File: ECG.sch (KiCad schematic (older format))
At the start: 8 parts

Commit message: Completed power circuits
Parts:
- gave numbers to parts that had none: 3
- renumbered 9V to 9V1, GND to GND1
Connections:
- net +9V: now reaches 9V1.1, C1.1, U2.1 (IN)
- net 2.5V: no longer names the net of C4.1, U1.6 (OUT)
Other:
- note added: "Voltage Reference"
- moved on the sheet: 9V1, C1, C2, C3, C4, GND1, U1, U2
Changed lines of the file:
@@
 encoding utf-8
 Sheet 1 1
-Title ""
+Title "Power"
 Date ""
 Rev ""
@@
 $EndDescr
 $Comp
-L Regulator_Linear:L7805 U?
+L Device:CP1 C2
+U 1 1 5F980DB6
+P 5825 2775
+F 0 "C2" H 5925 2875 50  0000 L CNN
+F 1 "10uF" H 5900 2700 50  0000 L CNN
+F 2 "" H 5825 2775 50  0001 C CNN
+F 3 "~" H 5825 2775 50  0001 C CNN
+	1    5825 2775
+	1    0    0    -1
+$EndComp
+$Comp
+L Device:CP1 C3
+U 1 1 5F9833A5
+P 6200 2775
+F 0 "C3" H 6315 2821 50  0000 L CNN
+F 1 "100nF" H 6315 2730 50  0000 L CNN
+F 2 "" H 6200 2775 50  0001 C CNN
+F 3 "~" H 6200 2775 50  0001 C CNN
+	1    6200 2775
+	1    0    0    -1
+$EndComp
+$Comp
+L Mechanical:MountingHole_Pad 9V1
+U 1 1 5F985E28
+P 4375 2625
+F 0 "9V1" V 4381 2777 50  0000 L CNN
+F 1 "MountingHole_Pad" V 4475 2583 50  0001 L CNN
+F 2 "" H 4375 2625 50  0001 C CNN
+F 3 "~" H 4375 2625 50  0001 C CNN
+	1    4375 2625
+	0    -1   -1   0
+$EndComp
+$Comp
+L Mechanical:MountingHole_Pad GND1
+U 1 1 5F98A564
+P 4375 2925
+F 0 "GND1" V 4475 2974 50  0000 L CNN
+F 1 "MountingHole_Pad" V 4475 2883 50  0001 L CNN
+F 2 "" H 4375 2925 50  0001 C CNN
+F 3 "~" H 4375 2925 50  0001 C CNN
+	1    4375 2925
+	0    -1   -1   0
+$EndComp
+Text Notes 4936 3380 0    118  ~ 0
+Input Power
+Text Notes 4808 5084 0    50   ~ 0
+Voltage Reference
+Wire Notes Line
+	3960 2350 3960 5784
+Wire Notes Line
+	3960 5784 6958 5784
+Wire Notes Line
+	6958 5784 6958 2118
+Wire Notes Line
+	6958 2118 3960 2118
+Wire Notes Line
+	3960 2118 3960 2348
+$Comp
+L power:GND #PWR0102
+U 1 1 5F9A88EF
+P 5400 2925
+F 0 "#PWR0102" H 5400 2675 50  0001 C CNN
+F 1 "GND" H 5405 2752 50  0000 C CNN
+F 2 "" H 5400 2925 50  0001 C CNN
+F 3 "" H 5400 2925 50  0001 C CNN
+	1    5400 2925
+	1    0    0    -1
+$EndComp
+$Comp
+L power:+9V #PWR0101
+U 1 1 5F9AB243
+P 4475 2625
+F 0 "#PWR0101" H 4475 2475 50  0001 C CNN
+F 1 "+9V" H 4490 2798 50  0000 C CNN
+F 2 "" H 4475 2625 50  0001 C CNN
+F 3 "" H 4475 2625 50  0001 C CNN
+	1    4475 2625
+	1    0    0    -1
+$EndComp
+$Comp
+L power:PWR_FLAG #FLG01
+U 1 1 5F9B3B5D
+P 4875 2625
+F 0 "#FLG01" H 4875 2700 50  0001 C CNN
+F 1 "PWR_FLAG" H 4875 2798 50  0000 C CNN
+F 2 "" H 4875 2625 50  0001 C CNN
+F 3 "~" H 4875 2625 50  0001 C CNN
+	1    4875 2625
+	1    0    0    -1
+$EndComp
+$Comp
+L Device:CP1 C4
+U 1 1 5F991542
+P 5475 4475
+F 0 "C4" H 5590 4521 50  0000 L CNN
+F 1 "1uF" H 5590 4430 50  0000 L CNN
+F 2 "" H 5475 4475 50  0001 C CNN
+F 3 "~" H 5475 4475 50  0001 C CNN
+	1    5475 4475
+	1    0    0    -1
+$EndComp
+Wire Wire Line
+	4825 4625 4750 4625
+Text GLabel 4750 4625 0    50   Input ~ 0
+5V
+$Comp
+L Reference_Voltage:ADR4525 U1
+U 1 1 5F98E0E5
+P 5125 4525
+F 0 "U1" V 4836 4525 50  0000 C CNN
+F 1 "ADR4525" V 4745 4525 50  0000 C CNN
+F 2 "Package_SO:SOIC-8_3.9x4.9mm_P1.27mm" H 5225 4225 50  0001 C CIN
+F 3 "https://www.analog.com/media/en/technical-documentation/data-sheets/ADR4520_4525_4530_4533_4540_4550.pdf" H 5225 4175 50  0001 C CIN
+	1    5125 4525
+	0    -1   -1   0
+$EndComp
+Wire Wire Line
+	5125 4225 5475 4225
+Wire Wire Line
+	5475 4225 5475 4325
+$Comp
+L power:GND #PWR02
+U 1 1 5F9D2687
+P 5475 4625
+F 0 "#PWR02" H 5475 4375 50  0001 C CNN
+F 1 "GND" H 5480 4452 50  0000 C CNN
+F 2 "" H 5475 4625 50  0001 C CNN
+F 3 "" H 5475 4625 50  0001 C CNN
+	1    5475 4625
+	1    0    0    -1
+$EndComp
+$Comp
+L Regulator_Linear:L7805 U2
 U 1 1 5F977B65
-P 2050 1200
-F 0 "U?" H 2050 1442 50  0000 C CNN
-F 1 "L7805" H 2050 1351 50  0000 C CNN
-F 2 "" H 2075 1050 50  0001 L CIN
-F 3 "http://www.st.com/content/ccc/resource/technical/document/datasheet/41/4f/b3/b0/12/d4/47/88/CD00000444.pdf/files/CD00000444.pdf/jcr:content/translations/en.CD00000444.pdf" H 2050 1150 50  0001 C CNN
-	1    2050 1200
+P 5400 2625
+F 0 "U2" H 5400 2867 50  0000 C CNN
+F 1 "L7805" H 5400 2776 50  0000 C CNN
+F 2 "" H 5425 2475 50  0001 L CIN
+F 3 "http://www.st.com/content/ccc/resource/technical/document/datasheet/41/4f/b3/b0/12/d4/47/88/CD00000444.pdf/files/CD00000444.pdf/jcr:content/translations/en.CD00000444.pdf" H 5400 2575 50  0001 C CNN
+	1    5400 2625
 	1    0    0    -1
 $EndComp
@@
 L Device:CP1 C1
 U 1 1 5F97B8CA
-P 1550 1350
-F 0 "C1" H 1665 1396 50  0000 L CNN
-F 1 "100uF" H 1665 1305 50  0000 L CNN
-F 2 "" H 1550 1350 50  0001 C CNN
-F 3 "~" H 1550 1350 50  0001 C CNN
-	1    1550 1350
-	1    0    0    -1
-$EndComp
-$Comp
-L Device:CP1 C2
-U 1 1 5F980DB6
-P 2550 1350
-F 0 "C2" H 2665 1396 50  0000 L CNN
-F 1 "10uF" H 2665 1305 50  0000 L CNN
-F 2 "" H 2550 1350 50  0001 C CNN
-F 3 "~" H 2550 1350 50  0001 C CNN
-	1    2550 1350
-	1    0    0    -1
-$EndComp
-$Comp
-L Device:CP1 C3
-U 1 1 5F9833A5
-P 2900 1350
-F 0 "C3" H 3015 1396 50  0000 L CNN
-F 1 "100nF" H 3015 1305 50  0000 L CNN
-F 2 "" H 2900 1350 50  0001 C CNN
-F 3 "~" H 2900 1350 50  0001 C CNN
-	1    2900 1350
-	1    0    0    -1
-$EndComp
-$Comp
-L power:GND #PWR?
-U 1 1 5F983C07
-P 2050 1500
-F 0 "#PWR?" H 2050 1250 50  0001 C CNN
-F 1 "GND" H 2055 1327 50  0000 C CNN
-F 2 "" H 2050 1500 50  0001 C CNN
-F 3 "" H 2050 1500 50  0001 C CNN
-	1    2050 1500
-	1    0    0    -1
-$EndComp
-Wire Wire Line
-	1550 1500 2050 1500
-Connection ~ 2050 1500
-Wire Wire Line
-	2900 1500 2550 1500
-Wire Wire Line
-	2050 1500 2550 1500
-Connection ~ 2550 1500
-Wire Wire Line
-	1550 1200 1750 1200
-Wire Wire Line
-	2350 1200 2550 1200
-Wire Wire Line
-	2900 1200 2550 1200
-Connection ~ 2550 1200
-$Comp
-L Mechanical:MountingHole_Pad 9V
-U 1 1 5F985E28
-P 1050 1200
-F 0 "9V" V 1150 1249 50  0000 L CNN
-F 1 "MountingHole_Pad" V 1150 1158 50  0001 L CNN
-F 2 "" H 1050 1200 50  0001 C CNN
-F 3 "~" H 1050 1200 50  0001 C CNN
-	1    1050 1200
-	0    -1   -1   0
-$EndComp
-$Comp
-L Mechanical:MountingHole_Pad GND
-U 1 1 5F98A564
-P 1050 1500
-F 0 "GND" V 1150 1549 50  0000 L CNN
-F 1 "MountingHole_Pad" V 1150 1458 50  0001 L CNN
-F 2 "" H 1050 1500 50  0001 C CNN
-F 3 "~" H 1050 1500 50  0001 C CNN
-	1    1050 1500
-	0    -1   -1   0
-$EndComp
-Wire Wire Line
-	1150 1200 1550 1200
-Connection ~ 1550 1200
-Wire Wire Line
-	1550 1500 1150 1500
-Connection ~ 1550 1500
-Text Label 2900 1200 0    50   ~ 0
+P 4875 2775
+F 0 "C1" H 4990 2821 50  0000 L CNN
+F 1 "100uF" H 4950 2700 50  0000 L CNN
+F 2 "" H 4875 2775 50  0001 C CNN
+F 3 "~" H 4875 2775 50  0001 C CNN
+	1    4875 2775
+	1    0    0    -1
+$EndComp
+Wire Wire Line
+	4475 2925 4875 2925
+Connection ~ 4875 2925
+Wire Wire Line
+	5400 2925 4875 2925
+Connection ~ 5400 2925
+Wire Wire Line
+	4875 2625 4475 2625
+Connection ~ 4875 2625
+Connection ~ 4475 2625
+Wire Wire Line
+	4875 2625 5100 2625
+Wire Wire Line
+	5700 2625 5825 2625
+Wire Wire Line
+	5400 2925 5825 2925
+Wire Wire Line
+	6200 2925 5825 2925
+Connection ~ 5825 2925
+Wire Wire Line
+	6200 2625 5825 2625
+Connection ~ 5825 2625
+Text GLabel 6200 2625 2    50   Input Italic 0
 5V
-Text Notes 1600 1950 0    118  ~ 0
-Input Power
-$Comp
-L Reference_Voltage:ADR4525 U?
-U 1 1 5F98E0E5
-P 1800 3100
-F 0 "U?" V 1511 3100 50  0000 C CNN
-F 1 "ADR4525" V 1420 3100 50  0000 C CNN
-F 2 "Package_SO:SOIC-8_3.9x4.9mm_P1.27mm" H 1900 2800 50  0001 C CIN
-F 3 "https://www.analog.com/media/en/technical-documentation/data-sheets/ADR4520_4525_4530_4533_4540_4550.pdf" H 1900 2750 50  0001 C CIN
-	1    1800 3100
-	0    -1   -1   0
-$EndComp
-Text Label 1400 3200 0    50   ~ 0
-5V
-Wire Wire Line
-	1400 3200 1500 3200
-Text Label 2200 3200 0    50   ~ 0
-GND
-Wire Wire Line
-	2100 3200 2200 3200
-$Comp
-L Device:CP1 C?
-U 1 1 5F991542
-P 2200 3000
-F 0 "C?" H 2315 3046 50  0000 L CNN
-F 1 "1uF" H 2315 2955 50  0000 L CNN
-F 2 "" H 2200 3000 50  0001 C CNN
-F 3 "~" H 2200 3000 50  0001 C CNN
-	1    2200 3000
-	1    0    0    -1
-$EndComp
-Wire Wire Line
-	2200 3150 2200 3200
-Wire Wire Line
-	1800 2800 2200 2800
-Wire Wire Line
-	2200 2800 2200 2850
-Text Label 2200 2800 0    50   ~ 0
-2.5V
+Wire Wire Line
+	5425 4625 5475 4625
+Connection ~ 5475 4625
+$Comp
+L power:PWR_FLAG #FLG?
+U 1 1 5F9F7887
+P 4875 2925
+F 0 "#FLG?" H 4875 3000 50  0001 C CNN
+F 1 "PWR_FLAG" H 4875 3098 50  0000 C CNN
+F 2 "" H 4875 2925 50  0001 C CNN
+F 3 "~" H 4875 2925 50  0001 C CNN
+	1    4875 2925
+	-1   0    0    1
+$EndComp
 $EndSCHEMATC

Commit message: First pass at schematic complete
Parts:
- added P1, P2, P3, Pgnd1, Vo1: MountingHole_Pad, symbol Mechanical:MountingHole_Pad
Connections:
- net GND: now also Pgnd1.1
- net 2.5V: now reaches C4.1, U1.6 (OUT)
- new net Filters_And_Gain/Vout: Vo1.1
- new net Probes/P1in: P1.1
- new net Probes/P2in: P2.1
- new net Probes/P3in: P3.1
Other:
- moved on the sheet: 9V1, C1, C2, C3, C4, GND1, U1, U2

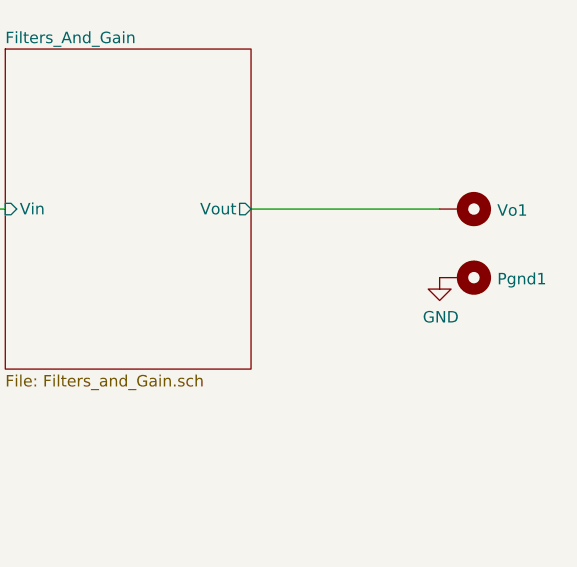
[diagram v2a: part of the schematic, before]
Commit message: Assigned footprints
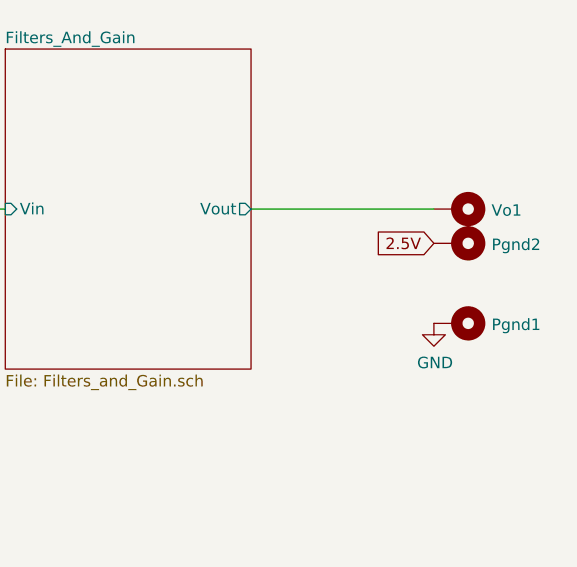
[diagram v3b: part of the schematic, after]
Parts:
- added Pgnd2: MountingHole_Pad, MountingHole:MountingHole_6mm_Pad_Via, symbol Mechanical:MountingHole_Pad
- 9V1: footprint (none) -> MountingHole:MountingHole_6.5mm_Pad_Via
- C1: footprint (none) -> Capacitor_SMD:CP_Elec_6.3x3
- C2: footprint (none) -> Capacitor_SMD:CP_Elec_5x5.3
- C3, C4: footprint (none) -> Capacitor_SMD:C_0805_2012Metric_Pad1.15x1.40mm_HandSolder
- GND1, P1, P2, P3, Pgnd1, Vo1: footprint (none) -> MountingHole:MountingHole_6mm_Pad_Via
- U2: footprint (none) -> Package_TO_SOT_THT:TO-220-3_Horizontal_TabDown
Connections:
- net 2.5V: now also Pgnd2.1
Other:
- moved on the sheet: Pgnd1, Vo1
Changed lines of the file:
@@
 F 0 "C2" H 2850 2525 50  0000 L CNN
 F 1 "10uF" H 2825 2350 50  0000 L CNN
-F 2 "" H 2750 2425 50  0001 C CNN
-F 3 "~" H 2750 2425 50  0001 C CNN
+F 2 "Capacitor_SMD:CP_Elec_5x5.3" H 2750 2425 50  0001 C CNN
+F 3 "https://www.illinoiscapacitor.com/pdf/seriesDocuments/AXZ%20series.pdf" H 2750 2425 50  0001 C CNN
 	1    2750 2425
 	1    0    0    -1
@@
 F 0 "C3" H 3240 2471 50  0000 L CNN
 F 1 "100nF" H 3240 2380 50  0000 L CNN
-F 2 "" H 3125 2425 50  0001 C CNN
+F 2 "Capacitor_SMD:C_0805_2012Metric_Pad1.15x1.40mm_HandSolder" H 3125 2425 50  0001 C CNN
 F 3 "~" H 3125 2425 50  0001 C CNN
 	1    3125 2425
@@
 F 0 "9V1" V 1306 2427 50  0000 L CNN
 F 1 "MountingHole_Pad" V 1400 2233 50  0001 L CNN
-F 2 "" H 1300 2275 50  0001 C CNN
+F 2 "MountingHole:MountingHole_6.5mm_Pad_Via" H 1300 2275 50  0001 C CNN
 F 3 "~" H 1300 2275 50  0001 C CNN
 	1    1300 2275
@@
 F 0 "GND1" V 1400 2624 50  0000 L CNN
 F 1 "MountingHole_Pad" V 1400 2533 50  0001 L CNN
-F 2 "" H 1300 2575 50  0001 C CNN
+F 2 "MountingHole:MountingHole_6mm_Pad_Via" H 1300 2575 50  0001 C CNN
 F 3 "~" H 1300 2575 50  0001 C CNN
 	1    1300 2575
@@
 F 0 "C4" H 2515 4171 50  0000 L CNN
 F 1 "1uF" H 2515 4080 50  0000 L CNN
-F 2 "" H 2400 4125 50  0001 C CNN
+F 2 "Capacitor_SMD:C_0805_2012Metric_Pad1.15x1.40mm_HandSolder" H 2400 4125 50  0001 C CNN
 F 3 "~" H 2400 4125 50  0001 C CNN
 	1    2400 4125
@@
 F 0 "U2" H 2325 2517 50  0000 C CNN
 F 1 "L7805" H 2325 2426 50  0000 C CNN
-F 2 "" H 2350 2125 50  0001 L CIN
+F 2 "Package_TO_SOT_THT:TO-220-3_Horizontal_TabDown" H 2350 2125 50  0001 L CIN
 F 3 "http://www.st.com/content/ccc/resource/technical/document/datasheet/41/4f/b3/b0/12/d4/47/88/CD00000444.pdf/files/CD00000444.pdf/jcr:content/translations/en.CD00000444.pdf" H 2325 2225 50  0001 C CNN
 	1    2325 2275
@@
 F 0 "C1" H 1915 2471 50  0000 L CNN
 F 1 "100uF" H 1875 2350 50  0000 L CNN
-F 2 "" H 1800 2425 50  0001 C CNN
-F 3 "~" H 1800 2425 50  0001 C CNN
+F 2 "Capacitor_SMD:CP_Elec_6.3x3" H 1800 2425 50  0001 C CNN
+F 3 "https://www.we-online.de/katalog/datasheet/860240575006.pdf" H 1800 2425 50  0001 C CNN
 	1    1800 2425
 	1    0    0    -1
@@
 	7375 3500 8375 3500
 $Comp
-L Mechanical:MountingHole_Pad Vo1
-U 1 1 5FA62E76
-P 10375 3500
-F 0 "Vo1" V 10381 3652 50  0000 L CNN
-F 1 "MountingHole_Pad" V 10475 3458 50  0001 L CNN
-F 2 "" H 10375 3500 50  0001 C CNN
-F 3 "~" H 10375 3500 50  0001 C CNN
-	1    10375 3500
-	0    1    1    0
-$EndComp
-$Comp
-L Mechanical:MountingHole_Pad Pgnd1
-U 1 1 5FA63F5B
-P 10375 3800
-F 0 "Pgnd1" V 10381 3952 50  0000 L CNN
-F 1 "MountingHole_Pad" V 10475 3758 50  0001 L CNN
-F 2 "" H 10375 3800 50  0001 C CNN
-F 3 "~" H 10375 3800 50  0001 C CNN
-	1    10375 3800
-	0    1    1    0
-$EndComp
-$Comp
-L power:GND #PWR03
-U 1 1 5FA65265
-P 10275 3800
-F 0 "#PWR03" H 10275 3550 50  0001 C CNN
-F 1 "GND" H 10280 3627 50  0000 C CNN
-F 2 "" H 10275 3800 50  0001 C CNN
-F 3 "" H 10275 3800 50  0001 C CNN
-	1    10275 3800
-	1    0    0    -1
-$EndComp
-Wire Wire Line
-	10275 3500 9450 3500
-$Comp
 L Mechanical:MountingHole_Pad P1
 U 1 1 5FA67DA7
@@
 F 0 "P1" V 5656 3327 50  0000 L CNN
 F 1 "MountingHole_Pad" V 5750 3133 50  0001 L CNN
-F 2 "" H 5650 3175 50  0001 C CNN
+F 2 "MountingHole:MountingHole_6mm_Pad_Via" H 5650 3175 50  0001 C CNN
 F 3 "~" H 5650 3175 50  0001 C CNN
 	1    5650 3175
@@
 F 0 "P2" V 5656 3577 50  0000 L CNN
 F 1 "MountingHole_Pad" V 5750 3383 50  0001 L CNN
-F 2 "" H 5650 3425 50  0001 C CNN
+F 2 "MountingHole:MountingHole_6mm_Pad_Via" H 5650 3425 50  0001 C CNN
 F 3 "~" H 5650 3425 50  0001 C CNN
 	1    5650 3425
@@
 F 0 "P3" V 5656 3827 50  0000 L CNN
 F 1 "MountingHole_Pad" V 5750 3633 50  0001 L CNN
-F 2 "" H 5650 3675 50  0001 C CNN
+F 2 "MountingHole:MountingHole_6mm_Pad_Via" H 5650 3675 50  0001 C CNN
 F 3 "~" H 5650 3675 50  0001 C CNN
 	1    5650 3675
@@
 Wire Wire Line
 	6425 3675 5750 3675
+Wire Wire Line
+	10250 3500 9450 3500
+$Comp
+L Mechanical:MountingHole_Pad Vo1
+U 1 1 5FA62E76
+P 10350 3500
+F 0 "Vo1" V 10356 3652 50  0000 L CNN
+F 1 "MountingHole_Pad" V 10450 3458 50  0001 L CNN
+F 2 "MountingHole:MountingHole_6mm_Pad_Via" H 10350 3500 50  0001 C CNN
+F 3 "~" H 10350 3500 50  0001 C CNN
+	1    10350 3500
+	0    1    1    0
+$EndComp
+$Comp
+L power:GND #PWR03
+U 1 1 5FA65265
+P 10250 4000
+F 0 "#PWR03" H 10250 3750 50  0001 C CNN
+F 1 "GND" H 10255 3827 50  0000 C CNN
+F 2 "" H 10250 4000 50  0001 C CNN
+F 3 "" H 10250 4000 50  0001 C CNN
+	1    10250 4000
+	1    0    0    -1
+$EndComp
+$Comp
+L Mechanical:MountingHole_Pad Pgnd1
+U 1 1 5FA63F5B
+P 10350 4000
+F 0 "Pgnd1" V 10356 4152 50  0000 L CNN
+F 1 "MountingHole_Pad" V 10450 3958 50  0001 L CNN
+F 2 "MountingHole:MountingHole_6mm_Pad_Via" H 10350 4000 50  0001 C CNN
+F 3 "~" H 10350 4000 50  0001 C CNN
+	1    10350 4000
+	0    1    1    0
+$EndComp
+Text GLabel 10250 3650 0    50   Input ~ 0
+2.5V
+$Comp
+L Mechanical:MountingHole_Pad Pgnd2
+U 1 1 5F9A2825
+P 10350 3650
+F 0 "Pgnd2" V 10356 3802 50  0000 L CNN
+F 1 "MountingHole_Pad" V 10450 3608 50  0001 L CNN
+F 2 "MountingHole:MountingHole_6mm_Pad_Via" H 10350 3650 50  0001 C CNN
+F 3 "~" H 10350 3650 50  0001 C CNN
+	1    10350 3650
+	0    1    1    0
+$EndComp
 $EndSCHEMATC
